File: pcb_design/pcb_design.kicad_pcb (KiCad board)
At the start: 4 copper layers, 72.9 x 60 mm, 91 parts, among them J1 PINHD_1x9_Female, J11 DB128L-5.08-2P-BK-S, J12 PINHD_1x4_Female, J2 PINHD_1x10_Female, J3 DB128L-5.08-2P-BK-S, J4 PINHD_1x3_Female, J5 PINHD_1x4_Female, Q11 MMUN2211LT1G, Q12 AO3401A, Q5 MMUN2211LT1G, Q6 AO3401A, Q7 MMUN2211LT1G, Q8 AO3401A, Q9 MMUN2211LT1G, SW1 KMR221GLFS, U1 L78M05CDT, U2 ESP32-S3-WROOM-1(N16R8), U3 L78M05CDT, U4 L78M05CDT

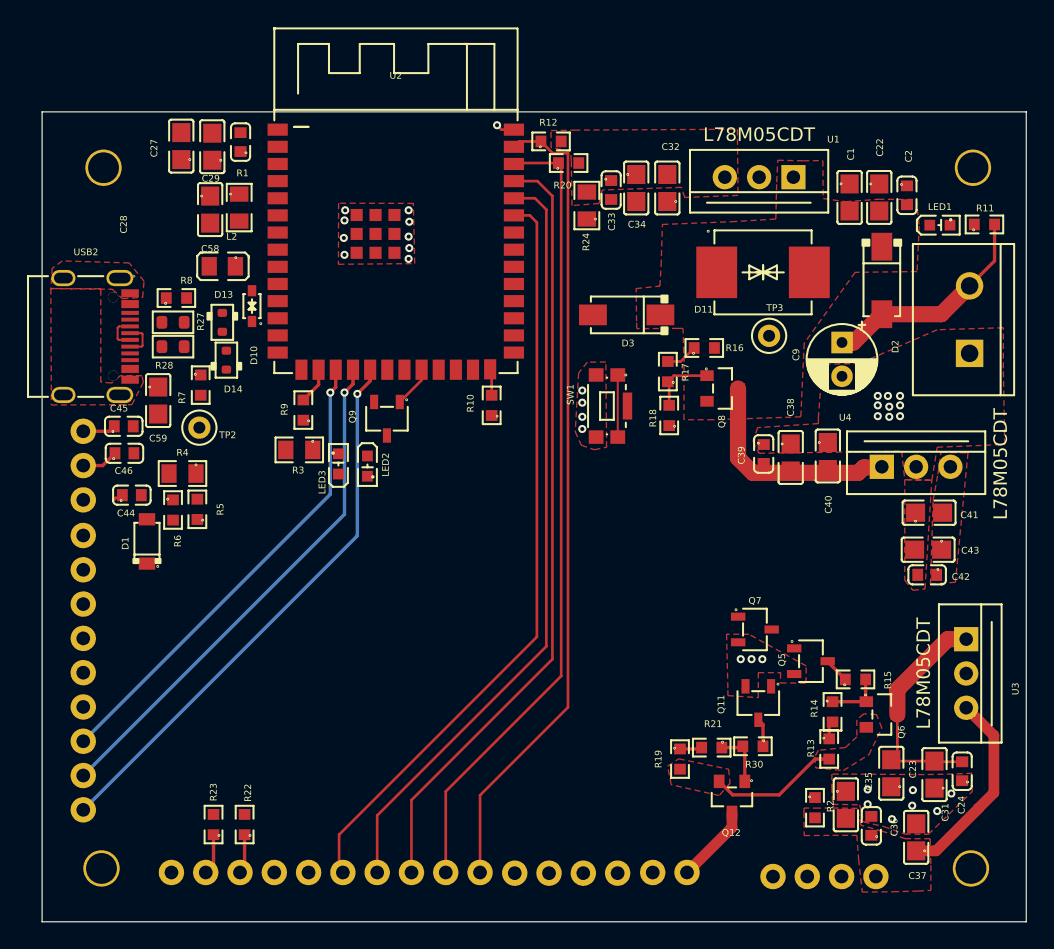
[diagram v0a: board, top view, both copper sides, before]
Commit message: terminacion de enrutado pcb de 4 capas, cambios en la huella de usb  y mountain hole capa de potencia solo para lineas delgadas de alimentacion, posible cambio para servo de 20kg
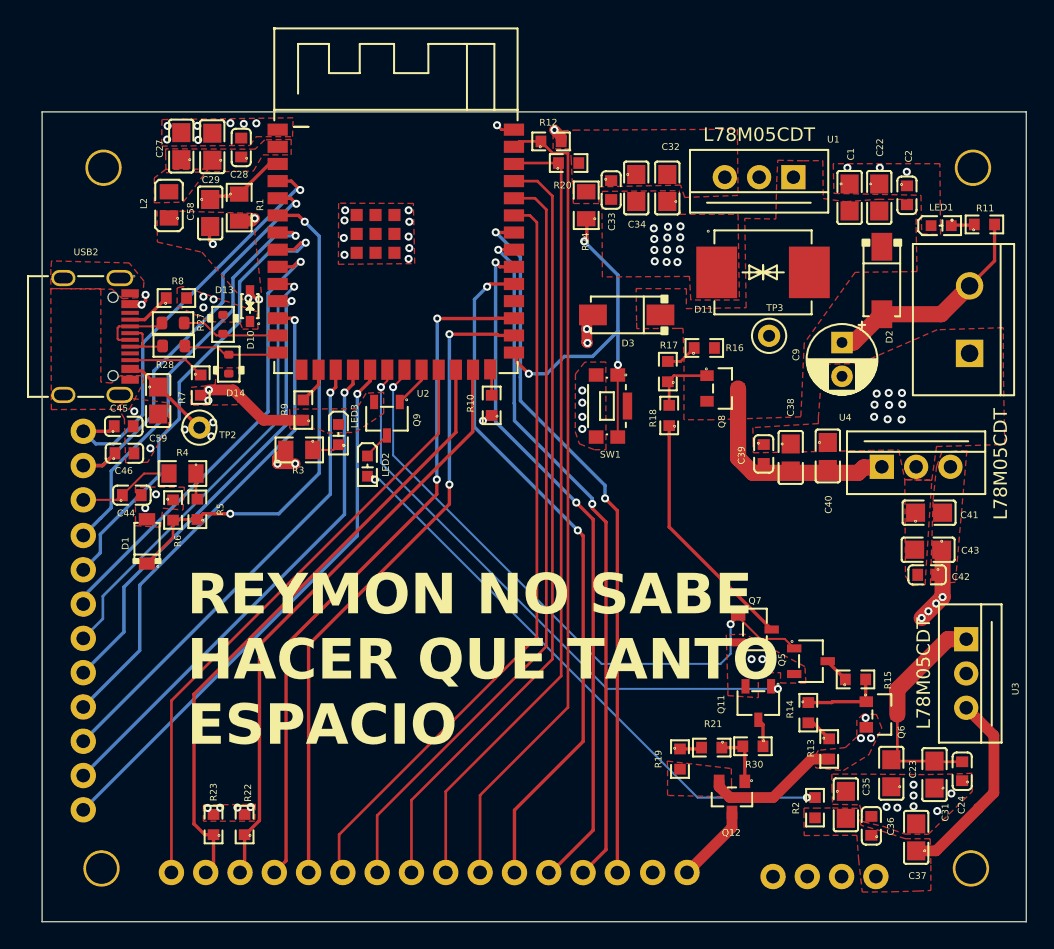
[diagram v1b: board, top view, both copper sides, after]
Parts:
- moved L2 6.03 mm to (108.2, 57.5), turned to 90 degrees
- moved LED3 2.17 mm to (120.7, 74.5), turned to -90 degrees
- moved R14 1.80 mm to (155.5, 95.1)
- moved C28 0.40 mm to (113.5, 53.2)
- moved D14 0.34 mm to (112.6, 69.2)
- moved C58 0.25 mm to (111.2, 58.0)
- moved D13 0.16 mm to (112.2, 66.3)
- moved D10 0.15 mm to (114.2, 65.0)
- moved LED1 0.10 mm to (165.3, 59.0)
- moved R28 0.07 mm to (108.5, 67.9)
- moved R24 0.05 mm to (139.1, 57.5)
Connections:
- J2 pad 4: /GPIO35 -> /GPIO36
- J2 pad 5: /GPIO36 -> /GPIO35
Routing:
- net +3.3v MICRO: track 0.00 -> 98.1 mm, vias 0 -> 6
- net +3.3V: track 0.00 -> 94.8 mm, vias 0 -> 8
- net VBUS: track 0.05 -> 58.2 mm, vias 0 -> 7
- net /GPIO41: track 0.00 -> 52.5 mm, vias 0 -> 2
- net /GPIO36: track 0.00 -> 51.7 mm, vias 0 -> 2
- net /GPIO40: track 0.00 -> 51.3 mm, vias 0 -> 2
- net /GPIO38: track 0.00 -> 51.3 mm, vias 0 -> 2
- net /GPIO39: track 0.00 -> 51.1 mm, vias 0 -> 2
- net /GPIO35: track 0.00 -> 49.0 mm, vias 0 -> 2
- net /source_control: track 0.00 -> 46.5 mm, vias 0 -> 2
- net /GPIO21: track 0.00 -> 45.4 mm
- net /TC: track 0.00 -> 44.0 mm, vias 0 -> 2
- net /GPIO47: track 3.04 -> 46.5 mm
- net Net-(LED2-A): track 0.00 -> 43.0 mm, vias 0 -> 2
- net /GPIO48: track 2.94 -> 44.4 mm
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- added copper zone on F.Cu, net Net-(U2-3V3)
- added copper zone on In2.Cu, net VCC
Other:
- board text added: "REYMON NO SABE HACER QUE TANTO ESPACIO"

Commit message: agregacion de islas de tierra para elimar acople de senales entre pistas
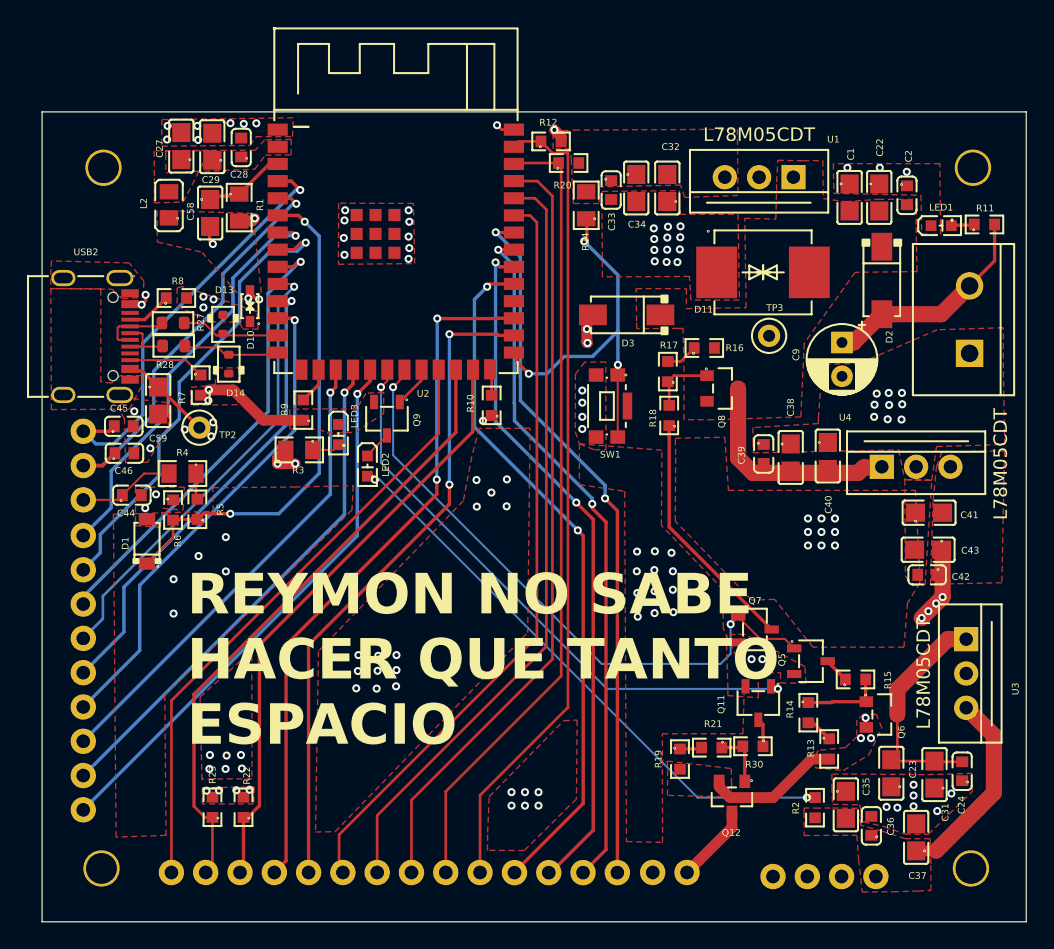
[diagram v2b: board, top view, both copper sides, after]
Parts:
- moved R22 1.28 mm to (113.7, 102.1)
- moved R23 1.28 mm to (111.4, 102.1)
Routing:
- net +3.3v MICRO: track 98.1 -> 98.9 mm
- net /GPIO47: track 46.5 -> 47.2 mm
- net /GPIO48: track 44.4 -> 45.1 mm
- net GND: vias 66 -> 119
